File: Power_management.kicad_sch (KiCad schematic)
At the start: 0 parts

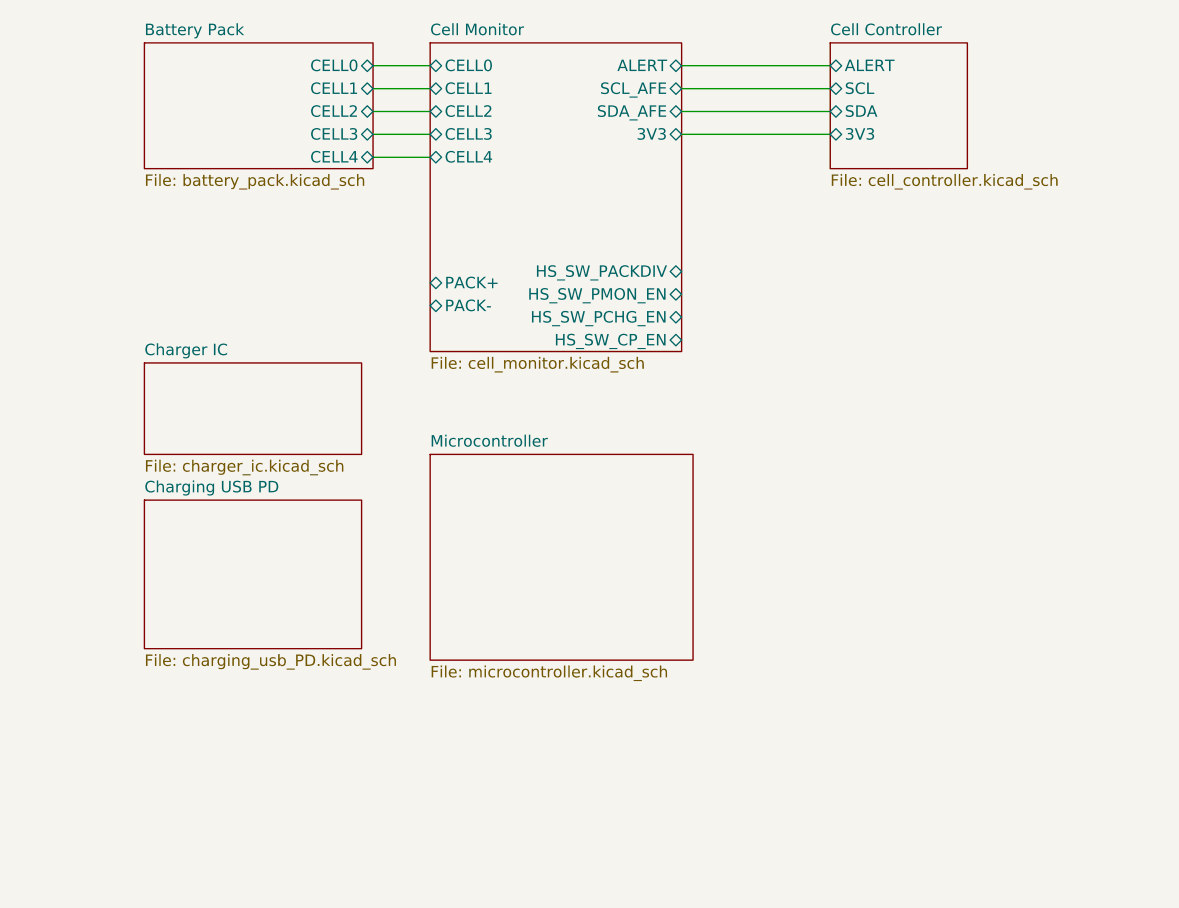
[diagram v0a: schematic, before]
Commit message: beginning fuel gage layout
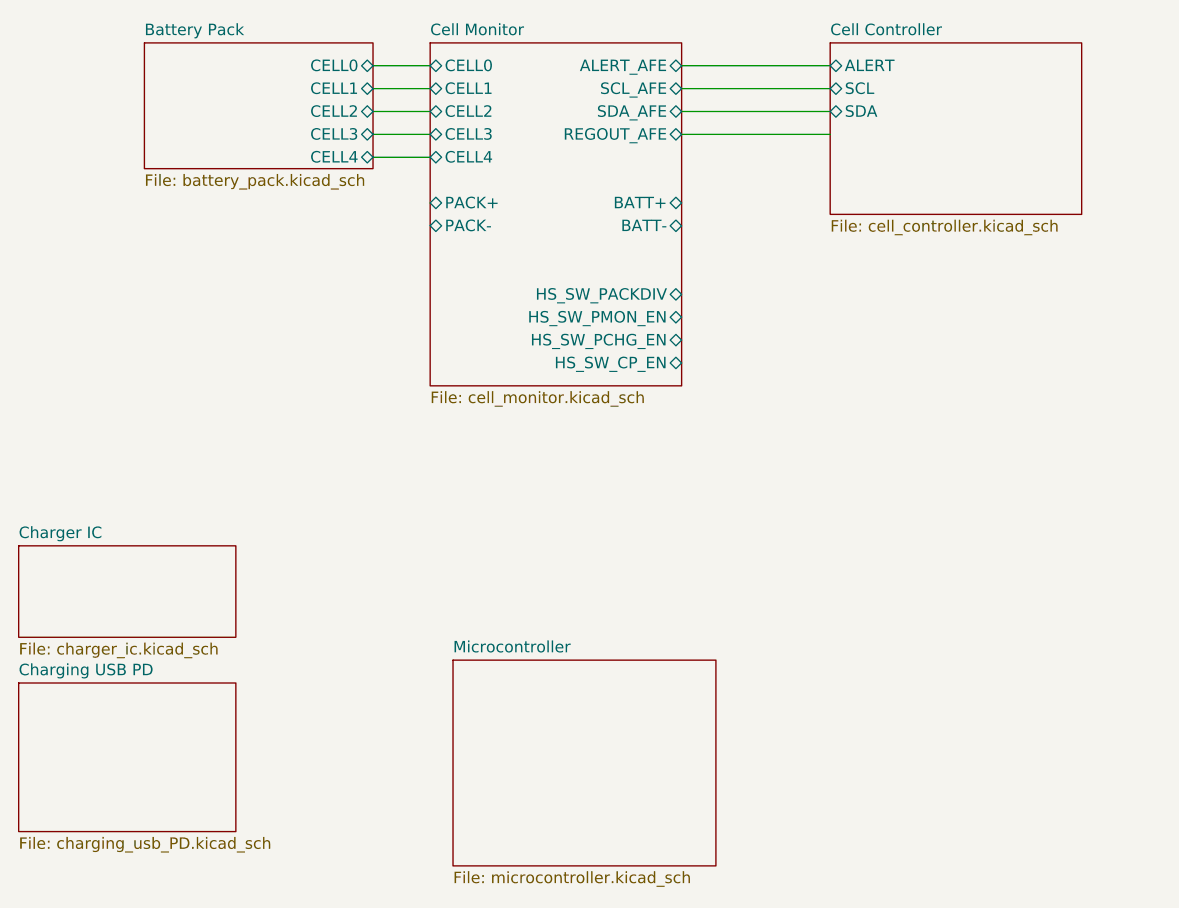
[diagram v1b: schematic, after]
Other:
- sheet Cell Controller ports: added none; removed 3V3
- sheet Cell Monitor ports: added ALERT_AFE, BATT+, BATT-, REGOUT_AFE; removed 3V3, ALERT
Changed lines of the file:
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@@
 	)
 	(sheet
-		(at 114.3 97.79)
+		(at 116.84 120.65)
 		(size 29.21 22.86)
 		(exclude_from_sim no)
@@
 		)
 		(property "Sheetname" "Microcontroller"
-			(at 114.3 97.0784 0)
+			(at 116.84 119.9384 0)
 			(effects
 				(font
@@
 		)
 		(property "Sheetfile" "microcontroller.kicad_sch"
-			(at 114.3 121.2346 0)
+			(at 116.84 144.0946 0)
 			(effects
 				(font
@@
 	)
 	(sheet
-		(at 82.55 87.63)
+		(at 68.58 107.95)
 		(size 24.13 10.16)
 		(exclude_from_sim no)
@@
 		)
 		(property "Sheetname" "Charger IC"
-			(at 82.55 86.9184 0)
+			(at 68.58 107.2384 0)
 			(effects
 				(font
@@
 		)
 		(property "Sheetfile" "charger_ic.kicad_sch"
-			(at 82.55 98.3746 0)
+			(at 68.58 118.6946 0)
 			(effects
 				(font
@@
 	)
 	(sheet
-		(at 82.55 102.87)
+		(at 68.58 123.19)
 		(size 24.13 16.51)
 		(exclude_from_sim no)
@@
 		)
 		(property "Sheetname" "Charging USB PD"
-			(at 82.55 102.1584 0)
+			(at 68.58 122.4784 0)
 			(effects
 				(font
@@
 		)
 		(property "Sheetfile" "charging_usb_PD.kicad_sch"
-			(at 82.55 119.9646 0)
+			(at 68.58 140.2846 0)
 			(effects
 				(font
@@
 	(sheet
 		(at 158.75 52.07)
-		(size 15.24 13.97)
+		(size 27.94 19.05)
 		(exclude_from_sim no)
 		(in_bom yes)
@@
 		)
 		(property "Sheetfile" "cell_controller.kicad_sch"
-			(at 158.75 66.6246 0)
+			(at 158.75 71.7046 0)
 			(effects
 				(font
@@
 		(pin "SCL" bidirectional
 			(at 158.75 57.15 180)
-			(effects
-				(font
-					(size 1.27 1.27)
-				)
-				(justify left)
-			)
-		)
-		(pin "3V3" bidirectional
-			(at 158.75 62.23 180)
 			(effects
 				(font
@@
 	(sheet
 		(at 114.3 52.07)
-		(size 27.94 34.29)
+		(size 27.94 38.1)
 		(exclude_from_sim no)
 		(in_bom yes)
@@
 		)
 		(property "Sheetfile" "cell_monitor.kicad_sch"
-			(at 114.3 86.9446 0)
+			(at 114.3 90.7546 0)
 			(effects
 				(font
@@
 		)
 		(pin "HS_SW_CP_EN" bidirectional
+			(at 142.24 87.63 0)
+			(effects
+				(font
+					(size 1.27 1.27)
+				)
+				(justify right)
+			)
+		)
+		(pin "PACK-" bidirectional
+			(at 114.3 72.39 180)
+			(effects
+				(font
+					(size 1.27 1.27)
+				)
+				(justify left)
+			)
+		)
+		(pin "HS_SW_PCHG_EN" bidirectional
 			(at 142.24 85.09 0)
-			(effects
-				(font
-					(size 1.27 1.27)
-				)
-				(justify right)
-			)
-		)
-		(pin "PACK-" bidirectional
-			(at 114.3 81.28 180)
-			(effects
-				(font
-					(size 1.27 1.27)
-				)
-				(justify left)
-			)
-		)
-		(pin "HS_SW_PCHG_EN" bidirectional
-			(at 142.24 82.55 0)
 			(effects
 				(font
@@
 		)
 		(pin "PACK+" bidirectional
-			(at 114.3 78.74 180)
-			(effects
-				(font
-					(size 1.27 1.27)
-				)
-				(justify left)
-			)
-		)
-		(pin "ALERT" bidirectional
-			(at 142.24 54.61 0)
-			(effects
-				(font
-					(size 1.27 1.27)
-				)
-				(justify right)
+			(at 114.3 69.85 180)
+			(effects
+				(font
+					(size 1.27 1.27)
+				)
+				(justify left)
 			)
 		)
@@
 			)
 		)
-		(pin "3V3" bidirectional
-			(at 142.24 62.23 0)
-			(effects
-				(font
-					(size 1.27 1.27)
-				)
-				(justify right)
-			)
-		)
 		(pin "CELL3" bidirectional
 			(at 114.3 62.23 180)
@@
 		)
 		(pin "HS_SW_PMON_EN" bidirectional
+			(at 142.24 82.55 0)
+			(effects
+				(font
+					(size 1.27 1.27)
+				)
+				(justify right)
+			)
+		)
+		(pin "HS_SW_PACKDIV" bidirectional
 			(at 142.24 80.01 0)
 			(effects
@@
 			)
 		)
-		(pin "HS_SW_PACKDIV" bidirectional
-			(at 142.24 77.47 0)
-			(effects
-				(font
+		(pin "ALERT_AFE" bidirectional
+			(at 142.24 54.61 0)
+			(effects
+				(font
+					(size 1.27 1.27)
+				)
+				(justify right)
+			)
+		)
+		(pin "BATT+" bidirectional
+			(at 142.24 69.85 0)
+			(effects
+				(font
+					(size 1.27 1.27)
+				)
+				(justify right)
+			)
+		)
+		(pin "BATT-" bidirectional
+			(at 142.24 72.39 0)
+			(effects
+				(font
+					(size 1.27 1.27)
+				)
+				(justify right)
+			)
+		)
+		(pin "REGOUT_AFE" bidirectional
+			(at 142.24 62.23 0)
+			(effects
+				(font

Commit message: .
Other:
- sheet Cell Controller ports: added ALERT_AFE, BATT+, BATT-, REGOUT_AFE, SCL_AFE, SDA_AFE; removed ALERT, SCL, SDA
- note added: "HS_SW = HIGHSIDE SWITCHING - referring to BQ76200PW high side switching driver"
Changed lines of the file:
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@@
 	(generator_version "9.0")
 	(paper "A4")
+	(text "HS_SW = HIGHSIDE SWITCHING - \nreferring to BQ76200PW high side switching driver"
+		(exclude_from_sim no)
+		(at 148.082 30.734 0)
+		(effects
+			(font
+				(size 1.27 1.27)
+			)
+		)
+	)
 	(wire
 		(pts
@@
 	(wire
 		(pts
+			(xy 142.24 69.85) (xy 158.75 69.85)
+		)
+		(stroke
+			(width 0)
+			(type default)
+		)
+	)
+	(wire
+		(pts
 			(xy 142.24 54.61) (xy 158.75 54.61)
 		)
@@
 		(pts
 			(xy 107.95 57.15) (xy 114.3 57.15)
+		)
+		(stroke
+			(width 0)
+			(type default)
+		)
+	)
+	(wire
+		(pts
+			(xy 142.24 72.39) (xy 158.75 72.39)
 		)
 		(stroke
@@
 	(sheet
 		(at 158.75 52.07)
-		(size 27.94 19.05)
+		(size 35.56 27.94)
 		(exclude_from_sim no)
 		(in_bom yes)
@@
 		)
 		(property "Sheetfile" "cell_controller.kicad_sch"
-			(at 158.75 71.7046 0)
+			(at 158.75 80.5946 0)
 			(effects
 				(font
@@
 			)
 		)
-		(pin "SCL" bidirectional
+		(pin "BATT-" bidirectional
+			(at 158.75 72.39 180)
+			(effects
+				(font
+					(size 1.27 1.27)
+				)
+				(justify left)
+			)
+		)
+		(pin "ALERT_AFE" bidirectional
+			(at 158.75 54.61 180)
+			(effects
+				(font
+					(size 1.27 1.27)
+				)
+				(justify left)
+			)
+		)
+		(pin "BATT+" bidirectional
+			(at 158.75 69.85 180)
+			(effects
+				(font
+					(size 1.27 1.27)
+				)
+				(justify left)
+			)
+		)
+		(pin "SDA_AFE" bidirectional
+			(at 158.75 59.69 180)
+			(effects
+				(font
+					(size 1.27 1.27)
+				)
+				(justify left)
+			)
+		)
+		(pin "SCL_AFE" bidirectional
 			(at 158.75 57.15 180)
 			(effects
@@
 			)
 		)
-		(pin "SDA" bidirectional
-			(at 158.75 59.69 180)
-			(effects
-				(font
-					(size 1.27 1.27)
-				)
-				(justify left)
-			)
-		)
-		(pin "ALERT" bidirectional
-			(at 158.75 54.61 180)
-			(effects
-				(font
+		(pin "REGOUT_AFE" bidirectional
+			(at 158.75 62.23 180)
+			(effects
+				(font

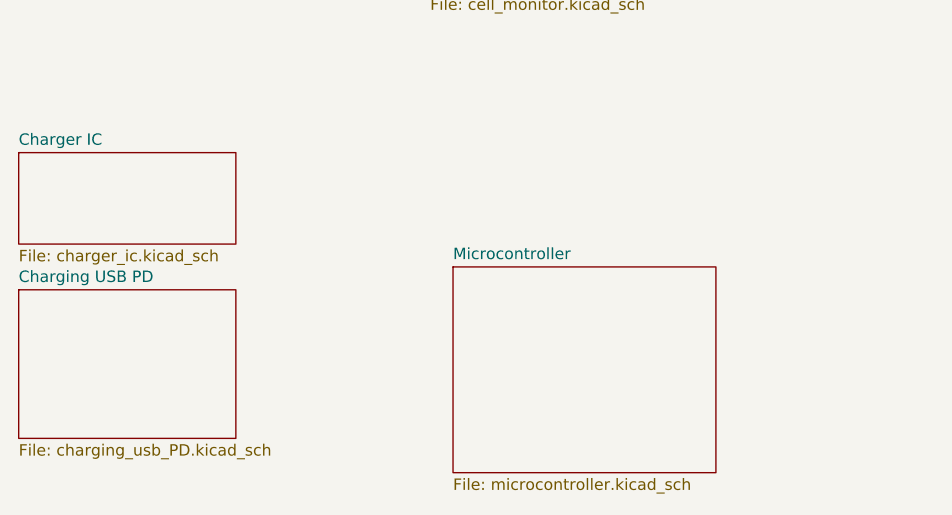
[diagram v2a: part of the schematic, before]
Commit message: starting usb pd charging
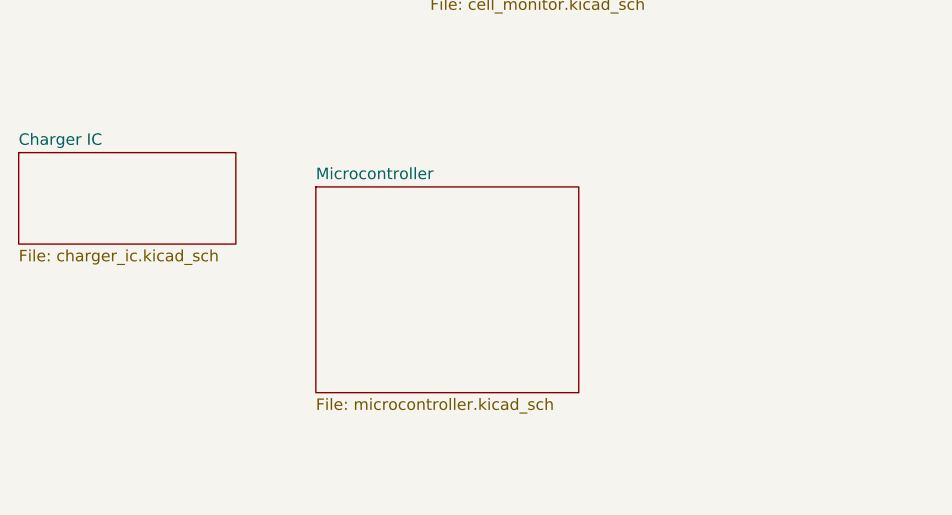
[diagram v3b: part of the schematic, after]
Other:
- removed sheet Charging USB PD
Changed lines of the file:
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@@
 	)
 	(sheet
-		(at 116.84 120.65)
+		(at 101.6 111.76)
 		(size 29.21 22.86)
 		(exclude_from_sim no)
@@
 		)
 		(property "Sheetname" "Microcontroller"
-			(at 116.84 119.9384 0)
+			(at 101.6 111.0484 0)
 			(effects
 				(font
@@
 		)
 		(property "Sheetfile" "microcontroller.kicad_sch"
-			(at 116.84 144.0946 0)
+			(at 101.6 135.2046 0)
 			(effects
 				(font
@@
 				)
 			)
-		)
-	)
-	(sheet
-		(at 68.58 123.19)
-		(size 24.13 16.51)
-		(exclude_from_sim no)
-		(in_bom yes)
-		(on_board yes)
-		(dnp no)
-		(fields_autoplaced yes)
-		(stroke
-			(width 0.1524)
-			(type solid)
-		)
-		(fill
-			(color 0 0 0 0.0000)
-		)
-		(property "Sheetname" "Charging USB PD"
-			(at 68.58 122.4784 0)
-			(effects
-				(font
-					(size 1.27 1.27)
-				)
-				(justify left bottom)
-			)
-		)
-		(property "Sheetfile" "charging_usb_PD.kicad_sch"
-			(at 68.58 140.2846 0)
-			(effects
-				(font
-					(size 1.27 1.27)
-				)
-				(justify left top)
-			)
-		)
-		(instances
-			(project "Power_management"
-				(path "/81e8a54f-a6a6-4f78-985c-1dc7d6751007"
-					(page "5")
-				)
-			)

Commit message: usb pd charging
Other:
- added sheet USB Interface (usb_interface.kicad_sch)
- sheet Battery Pack ports: added CELL5; removed none
- sheet Cell Monitor ports: added CELL5; removed none
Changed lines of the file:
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@@
+	(wire
+		(pts
+			(xy 107.95 67.31) (xy 114.3 67.31)
+		)
+		(stroke
+			(width 0)
+			(type default)
+		)
+	)
 	(wire
 		(pts
@@
 	)
 	(sheet
+		(at 142.24 101.6)
+		(size 25.4 16.51)
+		(exclude_from_sim no)
+		(in_bom yes)
+		(on_board yes)
+		(dnp no)
+		(fields_autoplaced yes)
+		(stroke
+			(width 0.1524)
+			(type solid)
+		)
+		(fill
+			(color 0 0 0 0.0000)
+		)
+		(property "Sheetname" "USB Interface"
+			(at 142.24 100.8884 0)
+			(effects
+				(font
+					(size 1.27 1.27)
+				)
+				(justify left bottom)
+			)
+		)
+		(property "Sheetfile" "usb_interface.kicad_sch"
+			(at 142.24 118.6946 0)
+			(effects
+				(font
+					(size 1.27 1.27)
+				)
+				(justify left top)
+			)
+		)
+		(instances
+			(project "Power_management"
+				(path "/81e8a54f-a6a6-4f78-985c-1dc7d6751007"
+					(page "7")
+				)
+			)
+		)
+	)
+	(sheet
 		(at 68.58 107.95)
 		(size 24.13 10.16)
@@
 	(sheet
 		(at 82.55 52.07)
-		(size 25.4 13.97)
+		(size 25.4 16.51)
 		(exclude_from_sim no)
 		(in_bom yes)
@@
 		)
 		(property "Sheetfile" "battery_pack.kicad_sch"
-			(at 82.55 66.6246 0)
+			(at 82.55 69.1646 0)
 			(effects
 				(font
@@
 		(pin "CELL4" bidirectional
 			(at 107.95 64.77 0)
+			(effects
+				(font
+					(size 1.27 1.27)
+				)
+				(justify right)
+			)
+		)
+		(pin "CELL5" bidirectional
+			(at 107.95 67.31 0)
 			(effects
 				(font
@@
 		)
 		(pin "PACK-" bidirectional
-			(at 114.3 72.39 180)
+			(at 114.3 85.09 180)
 			(effects
 				(font
@@
 		)
 		(pin "PACK+" bidirectional
-			(at 114.3 69.85 180)
+			(at 114.3 82.55 180)
 			(effects
 				(font
@@
 			)
 		)
+		(pin "CELL5" bidirectional
+			(at 114.3 67.31 180)
+			(effects
+				(font
+					(size 1.27 1.27)
+				)
+				(justify left)
+			)
+		)

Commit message: progress
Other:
- sheet Battery Pack ports: added BATT+, BATT-; removed none
- sheet Cell Monitor ports: added none; removed BATT+, BATT-
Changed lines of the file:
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@@
 	(wire
 		(pts
-			(xy 107.95 67.31) (xy 114.3 67.31)
-		)
-		(stroke
-			(width 0)
-			(type default)
-		)
-	)
-	(wire
-		(pts
-			(xy 107.95 54.61) (xy 114.3 54.61)
+			(xy 105.41 67.31) (xy 114.3 67.31)
+		)
+		(stroke
+			(width 0)
+			(type default)
+		)
+	)
+	(wire
+		(pts
+			(xy 151.13 81.28) (xy 105.41 81.28)
+		)
+		(stroke
+			(width 0)
+			(type default)
+		)
+	)
+	(wire
+		(pts
+			(xy 105.41 54.61) (xy 114.3 54.61)
 		)
 		(stroke
@@
 	(wire
 		(pts
+			(xy 105.41 83.82) (xy 153.67 83.82)
+		)
+		(stroke
+			(width 0)
+			(type default)
+		)
+	)
+	(wire
+		(pts
 			(xy 142.24 62.23) (xy 158.75 62.23)
 		)
@@
 	(wire
 		(pts
-			(xy 107.95 62.23) (xy 114.3 62.23)
-		)
-		(stroke
-			(width 0)
-			(type default)
-		)
-	)
-	(wire
-		(pts
-			(xy 142.24 69.85) (xy 158.75 69.85)
+			(xy 153.67 83.82) (xy 153.67 72.39)
+		)
+		(stroke
+			(width 0)
+			(type default)
+		)
+	)
+	(wire
+		(pts
+			(xy 105.41 62.23) (xy 114.3 62.23)
+		)
+		(stroke
+			(width 0)
+			(type default)
+		)
+	)
+	(wire
+		(pts
+			(xy 158.75 69.85) (xy 151.13 69.85)
 		)
 		(stroke
@@
 	(wire
 		(pts
-			(xy 107.95 64.77) (xy 114.3 64.77)
-		)
-		(stroke
-			(width 0)
-			(type default)
-		)
-	)
-	(wire
-		(pts
-			(xy 107.95 59.69) (xy 114.3 59.69)
-		)
-		(stroke
-			(width 0)
-			(type default)
-		)
-	)
-	(wire
-		(pts
-			(xy 107.95 57.15) (xy 114.3 57.15)
-		)
-		(stroke
-			(width 0)
-			(type default)
-		)
-	)
-	(wire
-		(pts
-			(xy 142.24 72.39) (xy 158.75 72.39)
+			(xy 105.41 64.77) (xy 114.3 64.77)
+		)
+		(stroke
+			(width 0)
+			(type default)
+		)
+	)
+	(wire
+		(pts
+			(xy 151.13 69.85) (xy 151.13 81.28)
+		)
+		(stroke
+			(width 0)
+			(type default)
+		)
+	)
+	(wire
+		(pts
+			(xy 105.41 59.69) (xy 114.3 59.69)
+		)
+		(stroke
+			(width 0)
+			(type default)
+		)
+	)
+	(wire
+		(pts
+			(xy 105.41 57.15) (xy 114.3 57.15)
+		)
+		(stroke
+			(width 0)
+			(type default)
+		)
+	)
+	(wire
+		(pts
+			(xy 153.67 72.39) (xy 158.75 72.39)
 		)
 		(stroke
@@
 	)
 	(sheet
-		(at 82.55 52.07)
-		(size 25.4 16.51)
+		(at 80.01 52.07)
+		(size 25.4 33.02)
 		(exclude_from_sim no)
 		(in_bom yes)
@@
 		)
 		(property "Sheetname" "Battery Pack"
-			(at 82.55 51.3584 0)
+			(at 80.01 51.3584 0)
 			(effects
 				(font
@@
 		)
 		(property "Sheetfile" "battery_pack.kicad_sch"
-			(at 82.55 69.1646 0)
+			(at 80.01 85.6746 0)
 			(effects
 				(font
@@
 		)
 		(pin "CELL2" bidirectional
-			(at 107.95 59.69 0)
+			(at 105.41 59.69 0)
 			(effects
 				(font
@@
 		)
 		(pin "CELL0" bidirectional
-			(at 107.95 54.61 0)
+			(at 105.41 54.61 0)
 			(effects
 				(font
@@
 		)
 		(pin "CELL3" bidirectional
-			(at 107.95 62.23 0)
+			(at 105.41 62.23 0)
 			(effects
 				(font
@@
 		)
 		(pin "CELL1" bidirectional
-			(at 107.95 57.15 0)
+			(at 105.41 57.15 0)
 			(effects
 				(font
@@
 		)
 		(pin "CELL4" bidirectional
-			(at 107.95 64.77 0)
+			(at 105.41 64.77 0)
 			(effects
 				(font
@@
 		)
 		(pin "CELL5" bidirectional
-			(at 107.95 67.31 0)
+			(at 105.41 67.31 0)
+			(effects
+				(font
+					(size 1.27 1.27)
+				)
+				(justify right)
+			)
+		)
+		(pin "BATT-" bidirectional
+			(at 105.41 83.82 0)
+			(effects
+				(font
+					(size 1.27 1.27)
+				)
+				(justify right)
+			)
+		)
+		(pin "BATT+" bidirectional
+			(at 105.41 81.28 0)
 			(effects
 				(font
@@
 	(sheet
 		(at 114.3 52.07)
-		(size 27.94 38.1)
+		(size 27.94 26.67)
 		(exclude_from_sim no)
 		(in_bom yes)
@@
 		)
 		(property "Sheetfile" "cell_monitor.kicad_sch"
-			(at 114.3 90.7546 0)
+			(at 114.3 79.3246 0)
 			(effects
 				(font
@@
 		)
 		(pin "HS_SW_CP_EN" bidirectional
-			(at 142.24 87.63 0)
+			(at 142.24 76.2 0)
 			(effects
 				(font
@@
 		)
 		(pin "PACK-" bidirectional
-			(at 114.3 85.09 180)
+			(at 114.3 73.66 180)
 			(effects
 				(font
@@
 		)
 		(pin "HS_SW_PCHG_EN" bidirectional
-			(at 142.24 85.09 0)
+			(at 142.24 73.66 0)
 			(effects
 				(font
@@
 		)
 		(pin "PACK+" bidirectional
-			(at 114.3 82.55 180)
+			(at 114.3 71.12 180)
 			(effects
 				(font
@@
 		)
 		(pin "HS_SW_PMON_EN" bidirectional
-			(at 142.24 82.55 0)
+			(at 142.24 71.12 0)
 			(effects
 				(font
@@
 		)
 		(pin "HS_SW_PACKDIV" bidirectional
-			(at 142.24 80.01 0)
+			(at 142.24 68.58 0)
 			(effects
 				(font
@@
 			(effects
 				(font
-					(size 1.27 1.27)
-				)
-				(justify right)
-			)
-		)
-		(pin "BATT+" bidirectional
-			(at 142.24 69.85 0)
-			(effects
-				(font
-					(size 1.27 1.27)
-				)
-				(justify right)
-			)
-		)
-		(pin "BATT-" bidirectional
-			(at 142.24 72.39 0)
-			(effects
-				(font

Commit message: progress on cell fuel gage
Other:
- note added: "REGOUT_AFE AT 3.3V?"
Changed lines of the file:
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@@
 	(generator_version "9.0")
 	(paper "A4")
+	(text "REGOUT_AFE AT 3.3V?"
+		(exclude_from_sim no)
+		(at 137.414 45.974 0)
+		(effects
+			(font
+				(size 1.27 1.27)
+			)
+		)
+	)
 	(text "HS_SW = HIGHSIDE SWITCHING - \nreferring to BQ76200PW high side switching driver"
 		(exclude_from_sim no)
